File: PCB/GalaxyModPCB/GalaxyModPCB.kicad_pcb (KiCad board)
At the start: 2 copper layers, 63.5 x 38.2 mm, 65 parts, among them J1 LED RGBW Connector, J2 USB to UART, J3 Motor Connector, J4 Projector Connector, J5 Debug Header, J6 Power Header, J7 Boot mode, Q1 IRLML0030, Q2 IRLML0030, Q3 IRLML0030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

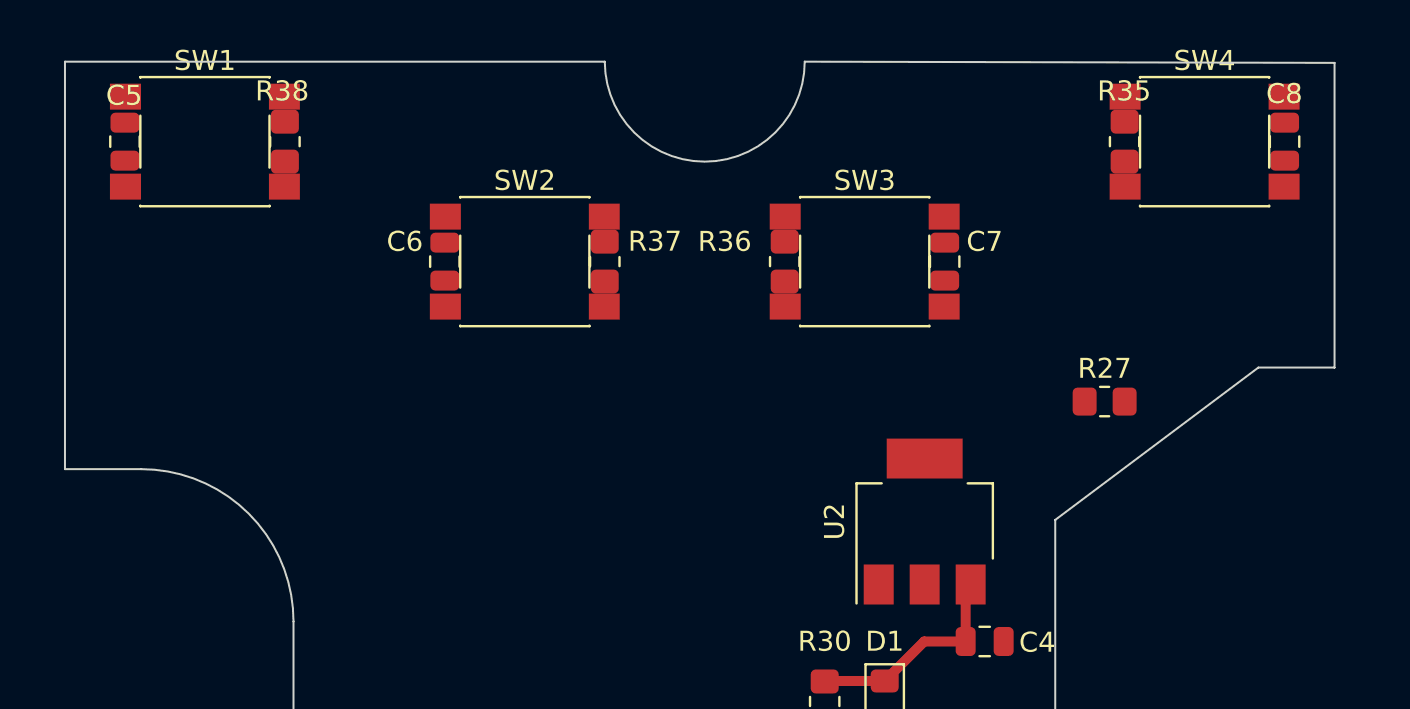
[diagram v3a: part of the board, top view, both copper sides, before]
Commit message: Connect switch peripherals
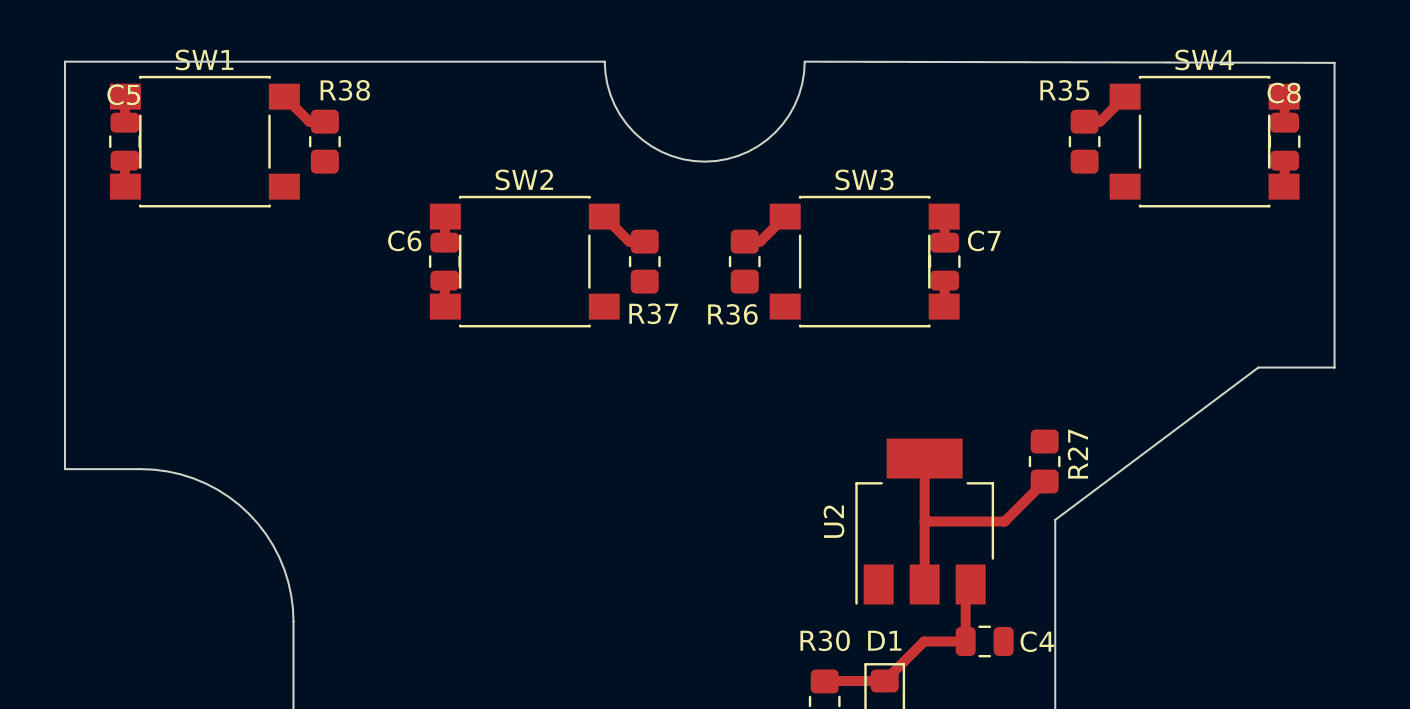
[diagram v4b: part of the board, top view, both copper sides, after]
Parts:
- moved R27 4.24 mm to (159.0, 71.0), turned to 90 degrees
- moved R35 2.00 mm to (161.0, 55.0)
- moved R36 2.00 mm to (144.0, 61.0)
- moved R37 2.00 mm to (139.0, 61.0)
- moved R38 2.00 mm to (123.0, 55.0)
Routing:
- net Net-(R27-Pad1): track 0.00 -> 13.1 mm
- net +3.3V: track 0.00 -> 5.24 mm
- net Net-(C8-Pad1): track 0.00 -> 3.85 mm
- net Net-(C7-Pad1): track 0.00 -> 3.85 mm
- net Net-(C6-Pad1): track 0.00 -> 3.85 mm
- net Net-(C5-Pad1): track 0.00 -> 3.85 mm
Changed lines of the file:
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@@
   )
   (footprint "Resistor_SMD:R_0805_2012Metric_Pad1.20x1.40mm_HandSolder" (layer "F.Cu")
-    (at 137 61 90)
+    (at 139 61 90)
     (descr "Resistor SMD 0805 (2012 Metric), square (rectangular) end terminal, IPC_7351 nominal with elongated pad for handsoldering. (Body size source: IPC-SM-782 page 72, https://www.pcb-3d.com/wordpress/wp-content/uploads/ipc-sm-782a_amendment_1_and_2.pdf), generated with kicad-footprint-generator")
     (tags "resistor handsolder")
@@
     (property "Sheetname" "")
     (attr smd)
-    (fp_text reference "R37" (at 1.008384 2.510655 180) (layer "F.SilkS")
-      (effects (font (size 1 1) (thickness 0.15)))
-    )
-    (fp_text value "10K" (at -0.807999 2.397131 180) (layer "F.Fab")
+    (fp_text reference "R37" (at -2.644638 0.438466 180) (layer "F.SilkS")
+      (effects (font (size 1 1) (thickness 0.15)))
+    )
+    (fp_text value "10K" (at -4.033955 0.335553 180) (layer "F.Fab")
       (effects (font (size 1 1) (thickness 0.15)))
     )
@@
   )
   (footprint "Resistor_SMD:R_0805_2012Metric_Pad1.20x1.40mm_HandSolder" (layer "F.Cu")
-    (at 163 55 90)
+    (at 161 55 90)
     (descr "Resistor SMD 0805 (2012 Metric), square (rectangular) end terminal, IPC_7351 nominal with elongated pad for handsoldering. (Body size source: IPC-SM-782 page 72, https://www.pcb-3d.com/wordpress/wp-content/uploads/ipc-sm-782a_amendment_1_and_2.pdf), generated with kicad-footprint-generator")
     (tags "resistor handsolder")
@@
     (property "Sheetname" "")
     (attr smd)
-    (fp_text reference "R35" (at 2.527624 -0.019594 180) (layer "F.SilkS")
-      (effects (font (size 1 1) (thickness 0.15)))
-    )
-    (fp_text value "10K" (at -2.751237 0.122311 180) (layer "F.Fab")
+    (fp_text reference "R35" (at 2.527624 -1 180) (layer "F.SilkS")
+      (effects (font (size 1 1) (thickness 0.15)))
+    )
+    (fp_text value "10K" (at 1 -3 180) (layer "F.Fab")
       (effects (font (size 1 1) (thickness 0.15)))
     )
@@
   )
   (footprint "Resistor_SMD:R_0805_2012Metric_Pad1.20x1.40mm_HandSolder" (layer "F.Cu")
-    (at 121 55 90)
+    (at 123 55 90)
     (descr "Resistor SMD 0805 (2012 Metric), square (rectangular) end terminal, IPC_7351 nominal with elongated pad for handsoldering. (Body size source: IPC-SM-782 page 72, https://www.pcb-3d.com/wordpress/wp-content/uploads/ipc-sm-782a_amendment_1_and_2.pdf), generated with kicad-footprint-generator")
     (tags "resistor handsolder")
@@
     (property "Sheetname" "")
     (attr smd)
-    (fp_text reference "R38" (at 2.527624 -0.136956 180) (layer "F.SilkS")
-      (effects (font (size 1 1) (thickness 0.15)))
-    )
-    (fp_text value "10K" (at -2.637713 0.175234 180) (layer "F.Fab")
+    (fp_text reference "R38" (at 2.527624 1 180) (layer "F.SilkS")
+      (effects (font (size 1 1) (thickness 0.15)))
+    )
+    (fp_text value "10K" (at 1 3 180) (layer "F.Fab")
       (effects (font (size 1 1) (thickness 0.15)))
     )
@@
   )
   (footprint "Resistor_SMD:R_0805_2012Metric_Pad1.20x1.40mm_HandSolder" (layer "F.Cu")
-    (at 162 68)
+    (at 159 71 90)
     (descr "Resistor SMD 0805 (2012 Metric), square (rectangular) end terminal, IPC_7351 nominal with elongated pad for handsoldering. (Body size source: IPC-SM-782 page 72, https://www.pcb-3d.com/wordpress/wp-content/uploads/ipc-sm-782a_amendment_1_and_2.pdf), generated with kicad-footprint-generator")
     (tags "resistor handsolder")
@@
     (property "Sheetname" "")
     (attr smd)
-    (fp_text reference "R27" (at 0 -1.65) (layer "F.SilkS")
-      (effects (font (size 1 1) (thickness 0.15)))
-    )
-    (fp_text value "0" (at 0 1.65) (layer "F.Fab")
-      (effects (font (size 1 1) (thickness 0.15)))
-    )
-    (fp_text user "${REFERENCE}" (at 0 0) (layer "F.Fab")
+    (fp_text reference "R27" (at 0.361456 1.709677 90) (layer "F.SilkS")
+      (effects (font (size 1 1) (thickness 0.15)))
+    )
+    (fp_text value "0" (at 0 3 90) (layer "F.Fab")
+      (effects (font (size 1 1) (thickness 0.15)))
+    )
+    (fp_text user "${REFERENCE}" (at 0 0 90) (layer "F.Fab")
       (effects (font (size 0.5 0.5) (thickness 0.08)))
     )
@@
     (fp_line (start 1 -0.625) (end 1 0.625) (layer "F.Fab") (width 0.1))
     (fp_line (start -1 0.625) (end -1 -0.625) (layer "F.Fab") (width 0.1))
-    (pad "1" smd roundrect (at -1 0) (size 1.2 1.4) (layers "F.Cu" "F.Paste" "F.Mask") (roundrect_rratio 0.208333)
+    (pad "1" smd roundrect (at -1 0 90) (size 1.2 1.4) (layers "F.Cu" "F.Paste" "F.Mask") (roundrect_rratio 0.208333)
       (net 36 "Net-(R27-Pad1)") (pintype "passive"))
-    (pad "2" smd roundrect (at 1 0) (size 1.2 1.4) (layers "F.Cu" "F.Paste" "F.Mask") (roundrect_rratio 0.208333)
+    (pad "2" smd roundrect (at 1 0 90) (size 1.2 1.4) (layers "F.Cu" "F.Paste" "F.Mask") (roundrect_rratio 0.208333)
       (net 9 "Net-(C10-Pad1)") (pintype "passive"))
     (model "${KICAD6_3DMODEL_DIR}/Resistor_SMD.3dshapes/R_0805_2012Metric.wrl"
@@
   )
   (footprint "Resistor_SMD:R_0805_2012Metric_Pad1.20x1.40mm_HandSolder" (layer "F.Cu")
-    (at 146 61 90)
+    (at 144 61 90)
     (descr "Resistor SMD 0805 (2012 Metric), square (rectangular) end terminal, IPC_7351 nominal with elongated pad for handsoldering. (Body size source: IPC-SM-782 page 72, https://www.pcb-3d.com/wordpress/wp-content/uploads/ipc-sm-782a_amendment_1_and_2.pdf), generated with kicad-footprint-generator")
     (tags "resistor handsolder")
@@
     (property "Sheetname" "")
     (attr smd)
-    (fp_text reference "R36" (at 1 -3 180) (layer "F.SilkS")
-      (effects (font (size 1 1) (thickness 0.15)))
-    )
-    (fp_text value "10K" (at -1 -3 180) (layer "F.Fab")
+    (fp_text reference "R36" (at -2.678943 -0.61656 180) (layer "F.SilkS")
+      (effects (font (size 1 1) (thickness 0.15)))
+    )
+    (fp_text value "10K" (at -3.982499 -0.633712 180) (layer "F.Fab")
       (effects (font (size 1 1) (thickness 0.15)))
     )
@@
   (segment (start 151 81.975) (end 152.975 80) (width 0.5) (layer "F.Cu") (net 3))
   (segment (start 148.025 81.975) (end 148 82) (width 0.5) (layer "F.Cu") (net 3))
+  (segment (start 113 54.05) (end 113 52.775) (width 0.5) (layer "F.Cu") (net 4))
+  (segment (start 123 54) (end 122.225 54) (width 0.5) (layer "F.Cu") (net 4))
+  (segment (start 113 52.775) (end 113.025 52.75) (width 0.5) (layer "F.Cu") (net 4))
+  (segment (start 122.225 54) (end 120.975 52.75) (width 0.5) (layer "F.Cu") (net 4))
+  (segment (start 154 61.95) (end 154 63.225) (width 0.5) (layer "F.Cu") (net 5))
+  (segment (start 113 55.95) (end 113 57.225) (width 0.5) (layer "F.Cu") (net 5))
+  (segment (start 171 55.95) (end 171 57.225) (width 0.5) (layer "F.Cu") (net 5))
+  (segment (start 113 57.225) (end 113.025 57.25) (width 0.5) (layer "F.Cu") (net 5))
+  (segment (start 129 63.225) (end 129.025 63.25) (width 0.5) (layer "F.Cu") (net 5))
+  (segment (start 171 57.225) (end 170.975 57.25) (width 0.5) (layer "F.Cu") (net 5))
+  (segment (start 129 61.95) (end 129 63.225) (width 0.5) (layer "F.Cu") (net 5))
+  (segment (start 154 63.225) (end 153.975 63.25) (width 0.5) (layer "F.Cu") (net 5))
+  (segment (start 139 60) (end 138.225 60) (width 0.5) (layer "F.Cu") (net 6))
+  (segment (start 138.225 60) (end 136.975 58.75) (width 0.5) (layer "F.Cu") (net 6))
+  (segment (start 129 58.775) (end 129.025 58.75) (width 0.5) (layer "F.Cu") (net 6))
+  (segment (start 129 60.05) (end 129 58.775) (width 0.5) (layer "F.Cu") (net 6))
+  (segment (start 154 58.775) (end 153.975 58.75) (width 0.5) (layer "F.Cu") (net 7))
+  (segment (start 144 60) (end 144.775 60) (width 0.5) (layer "F.Cu") (net 7))
+  (segment (start 144.775 60) (end 146.025 58.75) (width 0.5) (layer "F.Cu") (net 7))
+  (segment (start 154 60.05) (end 154 58.775) (width 0.5) (layer "F.Cu") (net 7))
+  (segment (start 171 54.05) (end 171 52.775) (width 0.5) (layer "F.Cu") (net 8))
+  (segment (start 161 54) (end 161.775 54) (width 0.5) (layer "F.Cu") (net 8))
+  (segment (start 161.775 54) (end 163.025 52.75) (width 0.5) (layer "F.Cu") (net 8))
+  (segment (start 171 52.775) (end 170.975 52.75) (width 0.5) (layer "F.Cu") (net 8))
   (segment (start 148 85.9375) (end 148.0625 86) (width 0.5) (layer "F.Cu") (net 10))
   (segment (start 148 84) (end 148 85.9375) (width 0.5) (layer "F.Cu") (net 10))
+  (segment (start 159 72) (end 157 74) (width 0.5) (layer "F.Cu") (net 36))
+  (segment (start 153 74) (end 153 77.15) (width 0.5) (layer "F.Cu") (net 36))
+  (segment (start 153 74) (end 153 70.85) (width 0.5) (layer "F.Cu") (net 36))
+  (segment (start 157 74) (end 153 74) (width 0.5) (layer "F.Cu") (net 36))
   (segment (start 151.025 84) (end 151 84.025) (width 0.5) (layer "F.Cu") (net 58))
   (segment (start 155 84) (end 151.025 84) (width 0.5) (layer "F.Cu") (net 58))

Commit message: Fixed motor diode footprint
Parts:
- D3: value 1N5817 -> Motor; footprint Diode_THT:D_DO-41_SOD81_P10.16mm_Horizontal -> Diode_SMD:D_0805_2012Metric_Pad1.15x1.40mm_HandSolder
- moved D3 20.2 mm to (65.0, 105.0)
- moved J3 7.94 mm to (56.0, 110.0)

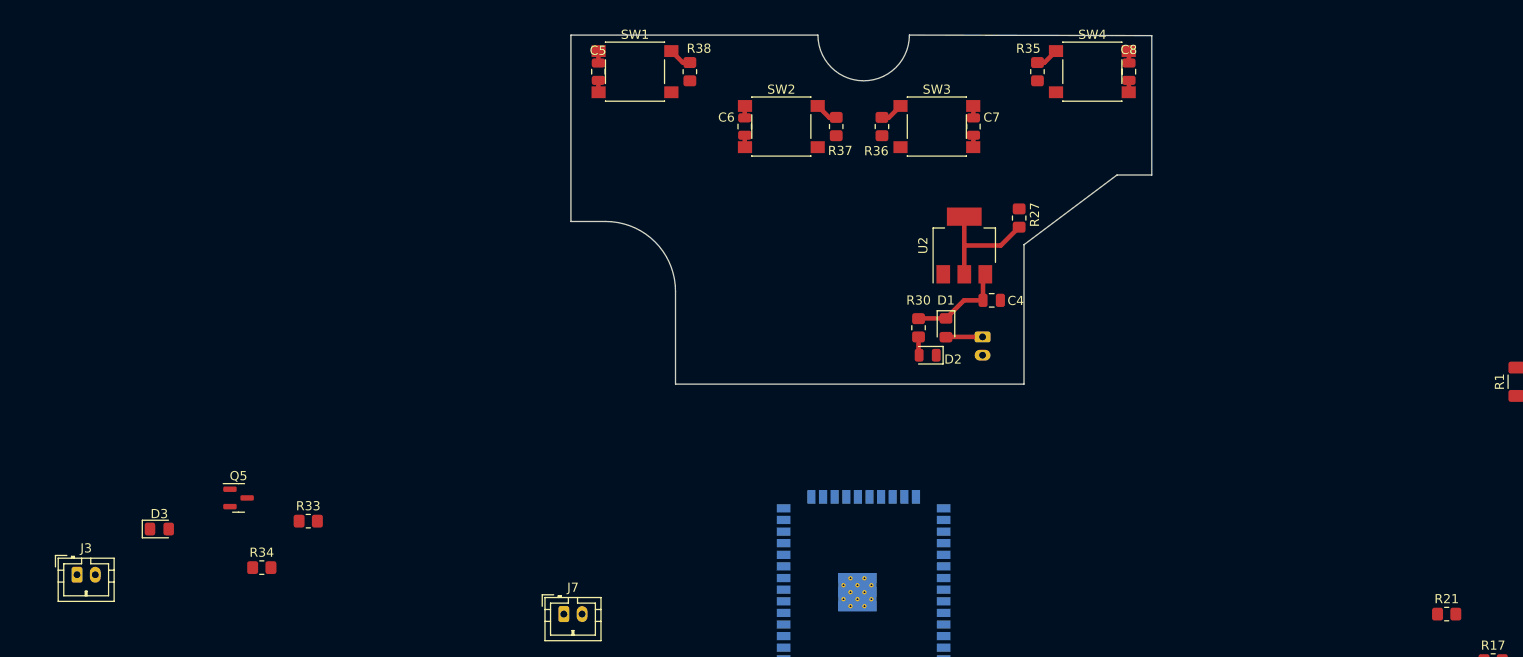
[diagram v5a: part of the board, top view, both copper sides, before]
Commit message: Fixed sketch trace connections
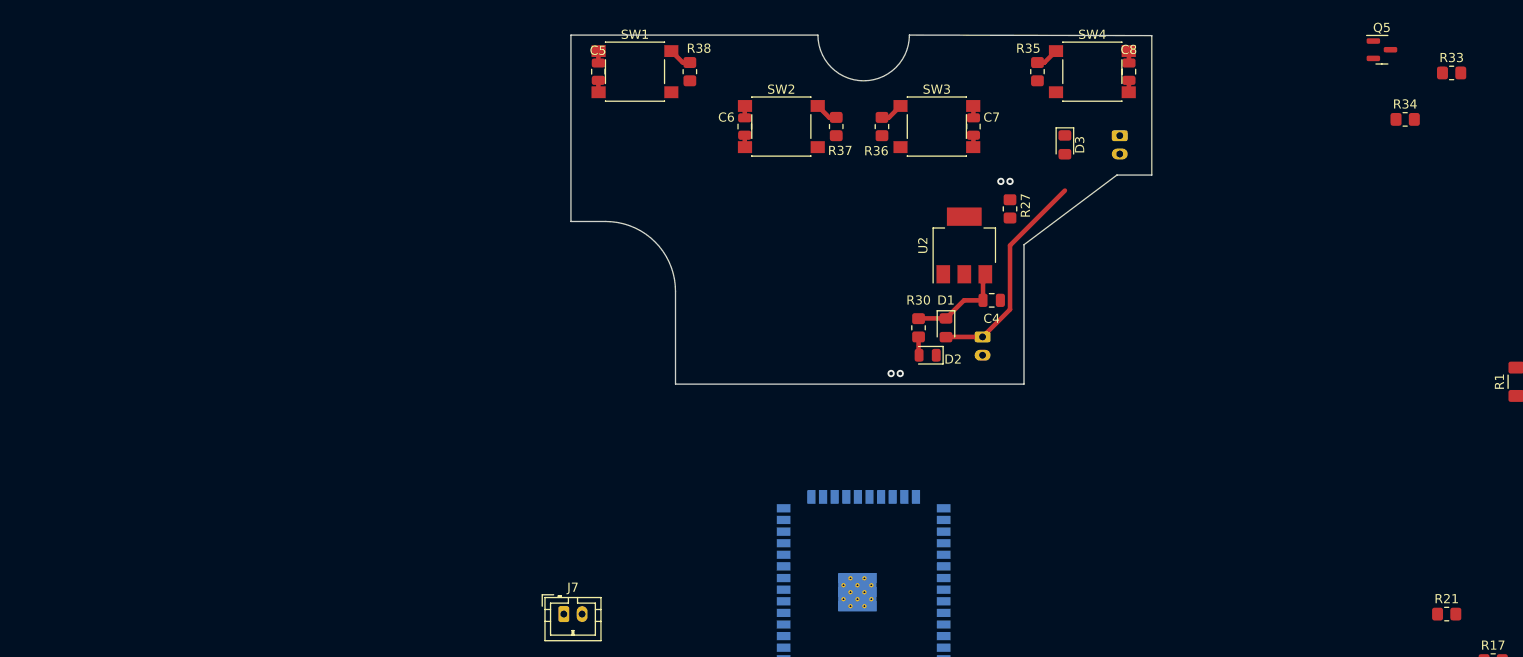
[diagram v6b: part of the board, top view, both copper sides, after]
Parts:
- J3: moved to B.Cu
- moved Q5 134.3 mm to (198.7, 52.6)
- moved R33 134.3 mm to (206.3, 55.1)
- moved R34 134.3 mm to (201.2, 60.2)
- moved J3 123.7 mm to (170.0, 62.0), turned to -90 degrees
- moved D3 107.5 mm to (164.0, 63.0), turned to -90 degrees
- moved R27 1.41 mm to (158.0, 70.0)
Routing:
- net Net-(J1-Pad1): track 4.01 -> 23.7 mm
- net Net-(R27-Pad1): track 13.1 -> 0.00 mm
- net (no net): vias 0 -> 4

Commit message: Fixed RVP of sketch
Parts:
- moved C4 11.4 mm to (145.0, 83.0), turned to -90 degrees
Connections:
- C6 pad 2: +3.3V -> Net-(C10-Pad1)
- C7 pad 2: +3.3V -> Net-(C10-Pad1)
- C8 pad 2: +3.3V -> Net-(C10-Pad1)
- D3 pad 1: VCC -> Net-(J1-Pad1)
- J3 pad 1: VCC -> Net-(J1-Pad1)
- J4 pad 1: +3.3V -> Net-(C10-Pad1)
- SW2 pad 2: +3.3V -> Net-(C10-Pad1)
- SW3 pad 2: +3.3V -> Net-(C10-Pad1)
- SW4 pad 2: +3.3V -> Net-(C10-Pad1)
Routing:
- net Net-(J1-Pad1): track 23.7 -> 36.9 mm
- net Net-(J3-Pad2): track 0.00 -> 6.01 mm
- net Net-(C10-Pad1): track 0.00 -> 3.93 mm
- net +3.3V: track 5.24 -> 1.31 mm
- net Net-(C4-Pad1): track 9.90 -> 11.8 mm
